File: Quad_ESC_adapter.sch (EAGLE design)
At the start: 14 parts, among them J1 284512-3, J2 284512-3, J3 284512-3, J4 284512-3

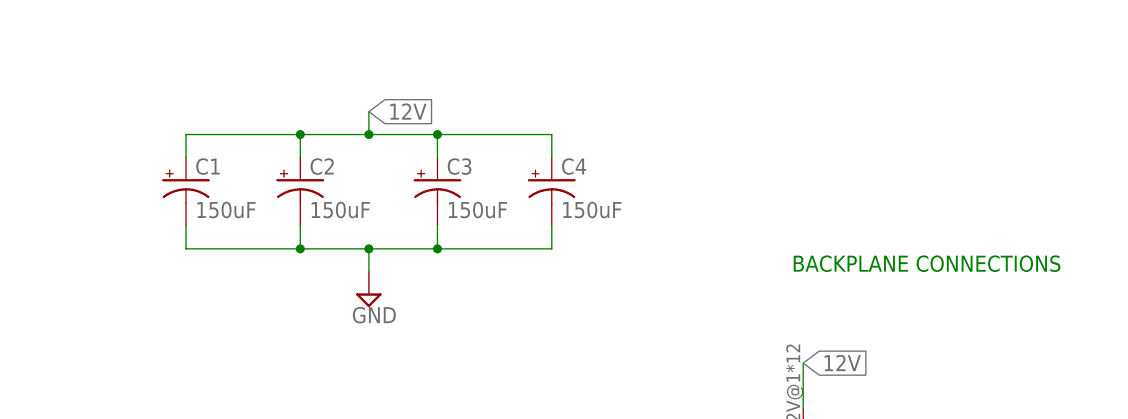
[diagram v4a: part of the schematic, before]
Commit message: Use aluminum caps for the adapter board
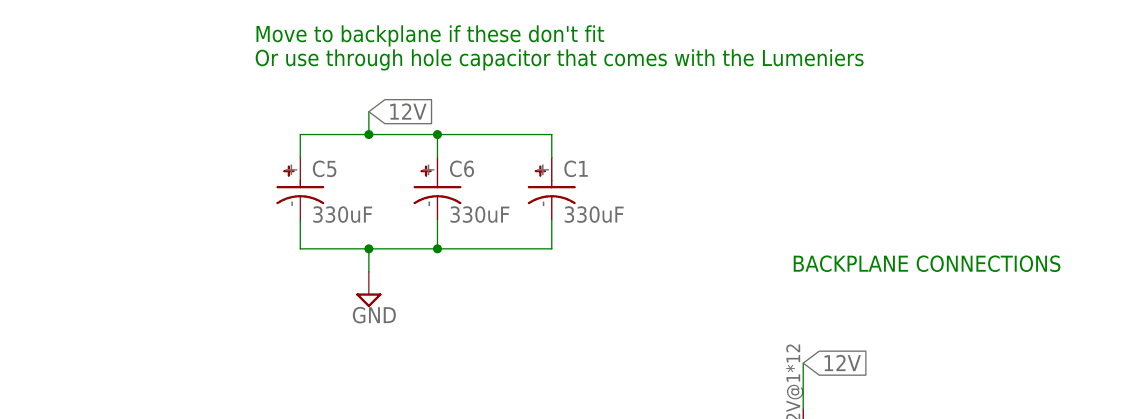
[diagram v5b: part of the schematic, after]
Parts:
- removed C2, C3, C4: 150uF, Tantalum Cap 150 uF - Kemet 2917 T491:C-TANTALUM(10UF_150UF)
- added C5, C6: 330uF, CAP, aluminin-capacitor-brick-UCM1H331MNL1GS:UCM1H331MNL1GS
- C1: value 150uF -> 330uF; device Tantalum Cap 150 uF - Kemet 2917 T491:C-TANTALUM(10UF_150UF) -> CAP, aluminin-capacitor-brick-UCM1H331MNL1GS:UCM1H331MNL1GS
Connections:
- net 12V: now also C5.+, C6.+; no longer C2.+, C3.+, C4.+
- net GND: now also C5.-, C6.-; no longer C2.-, C3.-, C4.-
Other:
- note added: "Move to backplane if these don't fit Or use through hole capacitor that comes with the Lumeniers"
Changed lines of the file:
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@@
 <part name="U$10" library="Lumenier ESC" deviceset="LUMENIER_QUAD-NO-CUT" device="" package3d_urn="urn:adsk.eagle:package:24294694/3"/>
 <part name="SUPPLY5" library="supply2" library_urn="urn:adsk.eagle:library:372" deviceset="GND" device=""/>
-<part name="C1" library="Tantalum Cap 150 uF - Kemet 2917 T491" deviceset="C-TANTALUM(10UF_150UF)" device="" package3d_urn="urn:adsk.eagle:package:25131320/3" value="150uF"/>
-<part name="C2" library="Tantalum Cap 150 uF - Kemet 2917 T491" deviceset="C-TANTALUM(10UF_150UF)" device="" package3d_urn="urn:adsk.eagle:package:25131320/3" value="150uF"/>
-<part name="C3" library="Tantalum Cap 150 uF - Kemet 2917 T491" deviceset="C-TANTALUM(10UF_150UF)" device="" package3d_urn="urn:adsk.eagle:package:25131320/3" value="150uF"/>
-<part name="C4" library="Tantalum Cap 150 uF - Kemet 2917 T491" deviceset="C-TANTALUM(10UF_150UF)" device="" package3d_urn="urn:adsk.eagle:package:25131320/3" value="150uF"/>
 <part name="SUPPLY1" library="supply2" library_urn="urn:adsk.eagle:library:372" deviceset="GND" device=""/>
 <part name="SUPPLY4" library="supply2" library_urn="urn:adsk.eagle:library:372" deviceset="GND" device=""/>
@@
 <part name="H4" library="Mounting Holes" deviceset="6-32-HOLE" device="" package3d_urn="urn:adsk.eagle:package:24384748/2"/>
 <part name="U$2" library="Backplane_ESC_adapter" deviceset="BACKPLANE_ESC_ADAPTER_PWR" device="ESC"/>
+<part name="C5" library="CAP, aluminin-capacitor-brick-UCM1H331MNL1GS" deviceset="UCM1H331MNL1GS" device="" package3d_urn="urn:adsk.eagle:package:24202090/2" value="330uF"/>
+<part name="C6" library="CAP, aluminin-capacitor-brick-UCM1H331MNL1GS" deviceset="UCM1H331MNL1GS" device="" package3d_urn="urn:adsk.eagle:package:24202090/2" value="330uF"/>
+<part name="C1" library="CAP, aluminin-capacitor-brick-UCM1H331MNL1GS" deviceset="UCM1H331MNL1GS" device="" package3d_urn="urn:adsk.eagle:package:24202090/2" value="330uF"/>
 </parts>
 <sheets>
@@
 <text x="209.55" y="91.44" size="1.778" layer="91">BACKPLANE CONNECTIONS</text>
 <text x="114.3" y="60.96" size="1.778" layer="91">LUMENIER ESC</text>
+<text x="149.86" y="114.3" size="1.778" layer="91">Move to backplane if these don't fit
+Or use through hole capacitor that comes with the Lumeniers</text>
 </plain>
 <instances>
@@
 <attribute name="VALUE" x="125.095" y="14.605" size="1.778" layer="96"/>
 </instance>
-<instance part="C1" gate="G$1" x="142.24" y="101.6" smashed="yes">
-<attribute name="NAME" x="143.256" y="102.235" size="1.778" layer="95"/>
-<attribute name="VALUE" x="143.256" y="97.409" size="1.778" layer="96"/>
-</instance>
-<instance part="C2" gate="G$1" x="154.94" y="101.6" smashed="yes">
-<attribute name="NAME" x="155.956" y="102.235" size="1.778" layer="95"/>
-<attribute name="VALUE" x="155.956" y="97.409" size="1.778" layer="96"/>
-</instance>
-<instance part="C3" gate="G$1" x="170.18" y="101.6" smashed="yes">
-<attribute name="NAME" x="171.196" y="102.235" size="1.778" layer="95"/>
-<attribute name="VALUE" x="171.196" y="97.409" size="1.778" layer="96"/>
-</instance>
-<instance part="C4" gate="G$1" x="182.88" y="101.6" smashed="yes">
-<attribute name="NAME" x="183.896" y="102.235" size="1.778" layer="95"/>
-<attribute name="VALUE" x="183.896" y="97.409" size="1.778" layer="96"/>
-</instance>
 <instance part="SUPPLY1" gate="GND" x="162.56" y="88.9" smashed="yes">
 <attribute name="VALUE" x="160.655" y="85.725" size="1.778" layer="96"/>
@@
 <instance part="U$2" gate="G$1" x="210.82" y="63.5" smashed="yes">
 <attribute name="NAME" x="208.28" y="60.96" size="1.27" layer="95" rot="R90"/>
+</instance>
+<instance part="C5" gate="G$1" x="154.94" y="101.6" smashed="yes">
+<attribute name="NAME" x="156.21" y="102.87" size="1.778" layer="95" align="center-left"/>
+<attribute name="VALUE" x="156.21" y="97.79" size="1.778" layer="95" align="center-left"/>
+</instance>
+<instance part="C6" gate="G$1" x="170.18" y="101.6" smashed="yes">
+<attribute name="NAME" x="171.45" y="102.87" size="1.778" layer="95" align="center-left"/>
+<attribute name="VALUE" x="171.45" y="97.79" size="1.778" layer="95" align="center-left"/>
+</instance>
+<instance part="C1" gate="G$1" x="182.88" y="101.6" smashed="yes">
+<attribute name="NAME" x="184.15" y="102.87" size="1.778" layer="95" align="center-left"/>
+<attribute name="VALUE" x="184.15" y="97.79" size="1.778" layer="95" align="center-left"/>
 </instance>
 </instances>
@@
 </segment>
 <segment>
-<pinref part="C1" gate="G$1" pin="-"/>
-<wire x1="142.24" y1="96.52" x2="142.24" y2="93.98" width="0.1524" layer="91"/>
-<wire x1="142.24" y1="93.98" x2="154.94" y2="93.98" width="0.1524" layer="91"/>
-<pinref part="C4" gate="G$1" pin="-"/>
 <wire x1="154.94" y1="93.98" x2="162.56" y2="93.98" width="0.1524" layer="91"/>
 <wire x1="162.56" y1="93.98" x2="170.18" y2="93.98" width="0.1524" layer="91"/>
 <wire x1="170.18" y1="93.98" x2="182.88" y2="93.98" width="0.1524" layer="91"/>
-<wire x1="182.88" y1="93.98" x2="182.88" y2="96.52" width="0.1524" layer="91"/>
-<pinref part="C3" gate="G$1" pin="-"/>
-<wire x1="170.18" y1="96.52" x2="170.18" y2="93.98" width="0.1524" layer="91"/>
+<wire x1="182.88" y1="93.98" x2="182.88" y2="97.155" width="0.1524" layer="91"/>
+<wire x1="170.18" y1="97.155" x2="170.18" y2="93.98" width="0.1524" layer="91"/>
 <junction x="170.18" y="93.98"/>
-<pinref part="C2" gate="G$1" pin="-"/>
-<wire x1="154.94" y1="96.52" x2="154.94" y2="93.98" width="0.1524" layer="91"/>
-<junction x="154.94" y="93.98"/>
+<wire x1="154.94" y1="97.155" x2="154.94" y2="93.98" width="0.1524" layer="91"/>
 <wire x1="162.56" y1="93.98" x2="162.56" y2="91.44" width="0.1524" layer="91"/>
 <junction x="162.56" y="93.98"/>
 <pinref part="SUPPLY1" gate="GND" pin="GND"/>
+<pinref part="C5" gate="G$1" pin="-"/>
+<pinref part="C6" gate="G$1" pin="-"/>
+<pinref part="C1" gate="G$1" pin="-"/>
 </segment>
 <segment>
@@
 </segment>
 <segment>
-<pinref part="C1" gate="G$1" pin="+"/>
-<wire x1="142.24" y1="104.14" x2="142.24" y2="106.68" width="0.1524" layer="91"/>
-<wire x1="142.24" y1="106.68" x2="154.94" y2="106.68" width="0.1524" layer="91"/>
-<pinref part="C4" gate="G$1" pin="+"/>
 <wire x1="154.94" y1="106.68" x2="162.56" y2="106.68" width="0.1524" layer="91"/>
 <wire x1="162.56" y1="106.68" x2="170.18" y2="106.68" width="0.1524" layer="91"/>
 <wire x1="170.18" y1="106.68" x2="182.88" y2="106.68" width="0.1524" layer="91"/>
 <wire x1="182.88" y1="106.68" x2="182.88" y2="104.14" width="0.1524" layer="91"/>
-<pinref part="C3" gate="G$1" pin="+"/>
 <wire x1="170.18" y1="104.14" x2="170.18" y2="106.68" width="0.1524" layer="91"/>
 <junction x="170.18" y="106.68"/>
-<pinref part="C2" gate="G$1" pin="+"/>
 <wire x1="154.94" y1="104.14" x2="154.94" y2="106.68" width="0.1524" layer="91"/>
-<junction x="154.94" y="106.68"/>
 <wire x1="162.56" y1="106.68" x2="162.56" y2="109.22" width="0.1524" layer="91"/>
 <junction x="162.56" y="106.68"/>
 <label x="162.56" y="109.22" size="1.778" layer="95" xref="yes"/>
+<pinref part="C5" gate="G$1" pin="+"/>
+<pinref part="C6" gate="G$1" pin="+"/>
+<pinref part="C1" gate="G$1" pin="+"/>
 </segment>
 <segment>
@@
 </drawing>
 <compatibility>
+<note version="6.3" minversion="6.2.2" severity="warning">
+Since Version 6.2.2 text objects can contain more than one line,
+which will not be processed correctly with this version.
+</note>
 <note version="8.2" severity="warning">
 Since Version 8.2, EAGLE supports online libraries. The ids
